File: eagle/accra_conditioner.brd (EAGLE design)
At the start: 160 x 100 mm, 25 parts, among them T1 PT204-6C

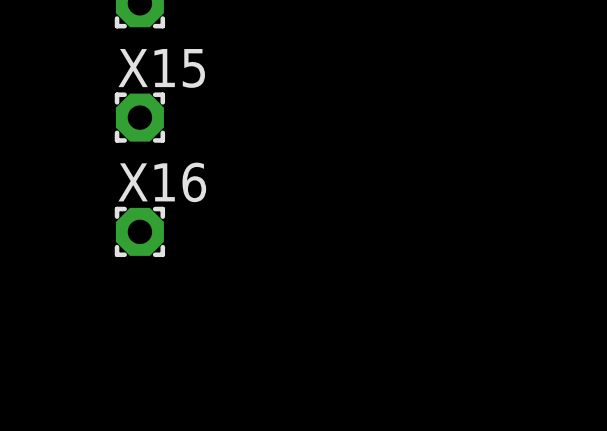
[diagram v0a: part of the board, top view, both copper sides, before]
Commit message: Fixed buffer amp.
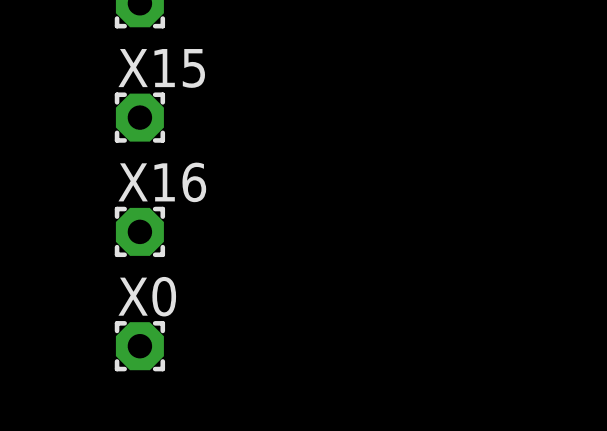
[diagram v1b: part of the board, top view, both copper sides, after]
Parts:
- added X0: (no value), wirepad:1,6/0,8
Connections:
- new net N$10: SO-1.13, SO-1.14, X15.1
- new net N$2: R3.1, SO-1.3, X1.1
- new net N$3: R4.1, SO-1.5, X3.1
- new net N$9: SO-1.8, SO-1.9, X13.1
- net +5V: now also X0.1
- net N$5: no longer R3.1, SO-1.3, X1.1
- net N$6: no longer R4.1, SO-1.5, X3.1
- net N$7: no longer SO-1.8, SO-1.9, X13.1
- net N$8: no longer SO-1.13, SO-1.14, X15.1
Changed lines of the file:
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@@
 <element name="X15" library="wirepad" package="1,6/0,8" value="" x="-17.78" y="-119.38"/>
 <element name="X16" library="wirepad" package="1,6/0,8" value="" x="-17.78" y="-123.19"/>
+<element name="X0" library="wirepad" package="1,6/0,8" value="" x="-17.78" y="-127"/>
 </elements>
 <signals>
@@
 </signal>
 <signal name="N$5">
-<contactref element="SO-1" pad="3"/>
-<contactref element="R3" pad="1"/>
 <contactref element="SO-1" pad="2"/>
 <contactref element="SO-1" pad="1"/>
-<contactref element="X1" pad="1"/>
 <contactref element="X9" pad="1"/>
-<wire x1="-17.78" y1="-66.04" x2="-17.78" y2="-96.52" width="0" layer="19" extent="1-1"/>
-<wire x1="-19.05" y1="-45.72" x2="-17.78" y2="-66.04" width="0" layer="19" extent="1-1"/>
-<wire x1="-17.78" y1="-40.7" x2="-19.05" y2="-45.72" width="0" layer="19" extent="1-1"/>
+<wire x1="-17.78" y1="-40.7" x2="-17.78" y2="-96.52" width="0" layer="19" extent="1-1"/>
 <wire x1="-16.51" y1="-40.7" x2="-17.78" y2="-40.7" width="0" layer="19" extent="1-1"/>
-<wire x1="-15.24" y1="-40.7" x2="-16.51" y2="-40.7" width="0" layer="19" extent="1-1"/>
 </signal>
 <signal name="N$6">
-<contactref element="SO-1" pad="5"/>
 <contactref element="SO-1" pad="6"/>
 <contactref element="SO-1" pad="7"/>
-<contactref element="R4" pad="1"/>
-<contactref element="X3" pad="1"/>
 <contactref element="X11" pad="1"/>
-<wire x1="-17.78" y1="-73.66" x2="-17.78" y2="-104.14" width="0" layer="19" extent="1-1"/>
-<wire x1="-19.05" y1="-50.8" x2="-17.78" y2="-73.66" width="0" layer="19" extent="1-1"/>
-<wire x1="-12.7" y1="-40.7" x2="-19.05" y2="-50.8" width="0" layer="19" extent="1-1"/>
-<wire x1="-11.43" y1="-40.7" x2="-12.7" y2="-40.7" width="0" layer="19" extent="1-1"/>
+<wire x1="-11.43" y1="-40.7" x2="-17.78" y2="-104.14" width="0" layer="19" extent="1-1"/>
 <wire x1="-10.16" y1="-40.7" x2="-11.43" y2="-40.7" width="0" layer="19" extent="1-1"/>
 </signal>
 <signal name="N$7">
 <contactref element="SO-1" pad="10"/>
-<contactref element="SO-1" pad="9"/>
-<contactref element="SO-1" pad="8"/>
 <contactref element="R5" pad="1"/>
 <contactref element="X5" pad="1"/>
-<contactref element="X13" pad="1"/>
-<wire x1="-17.78" y1="-81.28" x2="-17.78" y2="-111.76" width="0" layer="19" extent="1-1"/>
 <wire x1="-19.05" y1="-55.88" x2="-17.78" y2="-81.28" width="0" layer="19" extent="1-1"/>
 <wire x1="-12.7" y1="-35.5" x2="-19.05" y2="-55.88" width="0" layer="19" extent="1-1"/>
-<wire x1="-11.43" y1="-35.5" x2="-12.7" y2="-35.5" width="0" layer="19" extent="1-1"/>
-<wire x1="-10.16" y1="-35.5" x2="-11.43" y2="-35.5" width="0" layer="19" extent="1-1"/>
 </signal>
 <signal name="N$8">
 <contactref element="SO-1" pad="12"/>
-<contactref element="SO-1" pad="13"/>
-<contactref element="SO-1" pad="14"/>
 <contactref element="R6" pad="1"/>
 <contactref element="X7" pad="1"/>
-<contactref element="X15" pad="1"/>
-<wire x1="-17.78" y1="-88.9" x2="-17.78" y2="-119.38" width="0" layer="19" extent="1-1"/>
 <wire x1="-19.05" y1="-60.96" x2="-17.78" y2="-88.9" width="0" layer="19" extent="1-1"/>
-<wire x1="-17.78" y1="-35.5" x2="-19.05" y2="-60.96" width="0" layer="19" extent="1-1"/>
-<wire x1="-16.51" y1="-35.5" x2="-17.78" y2="-35.5" width="0" layer="19" extent="1-1"/>
-<wire x1="-15.24" y1="-35.5" x2="-16.51" y2="-35.5" width="0" layer="19" extent="1-1"/>
+<wire x1="-15.24" y1="-35.5" x2="-19.05" y2="-60.96" width="0" layer="19" extent="1-1"/>
 </signal>
 <signal name="+5V">
@@
 <contactref element="R5" pad="2"/>
 <contactref element="R4" pad="2"/>
+<contactref element="X0" pad="1"/>
+<wire x1="-8.89" y1="-60.96" x2="-17.78" y2="-127" width="0" layer="19" extent="1-1"/>
 <wire x1="-8.89" y1="-55.88" x2="-8.89" y2="-60.96" width="0" layer="19" extent="1-1"/>
 <wire x1="-8.89" y1="-50.8" x2="-8.89" y2="-55.88" width="0" layer="19" extent="1-1"/>
@@
 <wire x1="2.54" y1="-3.81" x2="-13.97" y2="-40.7" width="0" layer="19" extent="1-1"/>
 </signal>
+<signal name="N$2">
+<contactref element="SO-1" pad="3"/>
+<contactref element="R3" pad="1"/>
+<contactref element="X1" pad="1"/>
+<wire x1="-19.05" y1="-45.72" x2="-17.78" y2="-66.04" width="0" layer="19" extent="1-1"/>
+<wire x1="-15.24" y1="-40.7" x2="-19.05" y2="-45.72" width="0" layer="19" extent="1-1"/>
+</signal>
+<signal name="N$3">
+<contactref element="SO-1" pad="5"/>
+<contactref element="R4" pad="1"/>
+<contactref element="X3" pad="1"/>
+<wire x1="-19.05" y1="-50.8" x2="-17.78" y2="-73.66" width="0" layer="19" extent="1-1"/>
+<wire x1="-12.7" y1="-40.7" x2="-19.05" y2="-50.8" width="0" layer="19" extent="1-1"/>
+</signal>
+<signal name="N$9">
+<contactref element="SO-1" pad="9"/>
+<contactref element="SO-1" pad="8"/>
+<contactref element="X13" pad="1"/>
+<wire x1="-11.43" y1="-35.5" x2="-17.78" y2="-111.76" width="0" layer="19" extent="1-1"/>
+<wire x1="-10.16" y1="-35.5" x2="-11.43" y2="-35.5" width="0" layer="19" extent="1-1"/>
+</signal>
+<signal name="N$10">
+<contactref element="SO-1" pad="13"/>
+<contactref element="SO-1" pad="14"/>
+<contactref element="X15" pad="1"/>
+<wire x1="-17.78" y1="-35.5" x2="-17.78" y2="-119.38" width="0" layer="19" extent="1-1"/>
+<wire x1="-16.51" y1="-35.5" x2="-17.78" y2="-35.5" width="0" layer="19" extent="1-1"/>
+</signal>
 </signals>
